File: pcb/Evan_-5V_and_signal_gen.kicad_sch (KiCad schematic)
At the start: 34 parts, among them IC1 TL7660IDGKR, IC2 TL081IDT, IC4 UA78M33CDCYG3, IC9 TL081IDT, J2 ESQ-126-39-L-D, J3 ESQ-126-39-L-D, U5 TPS2069CDBVR_MOSFET

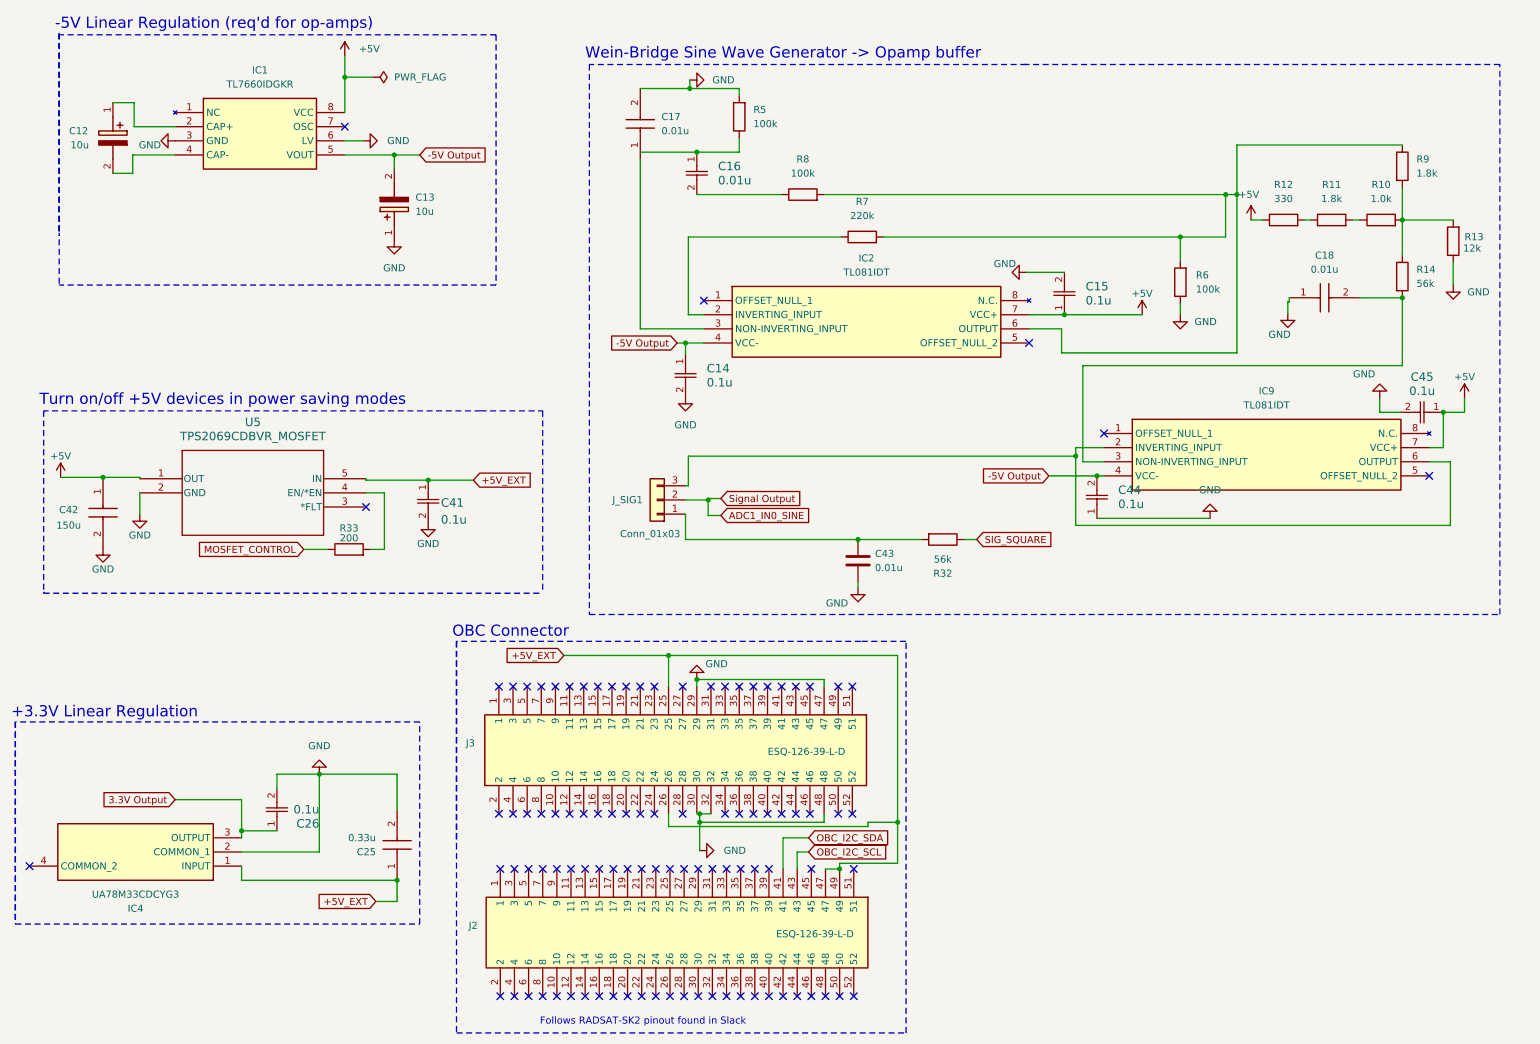
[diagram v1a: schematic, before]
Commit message: Added LM35 Temp Sensor
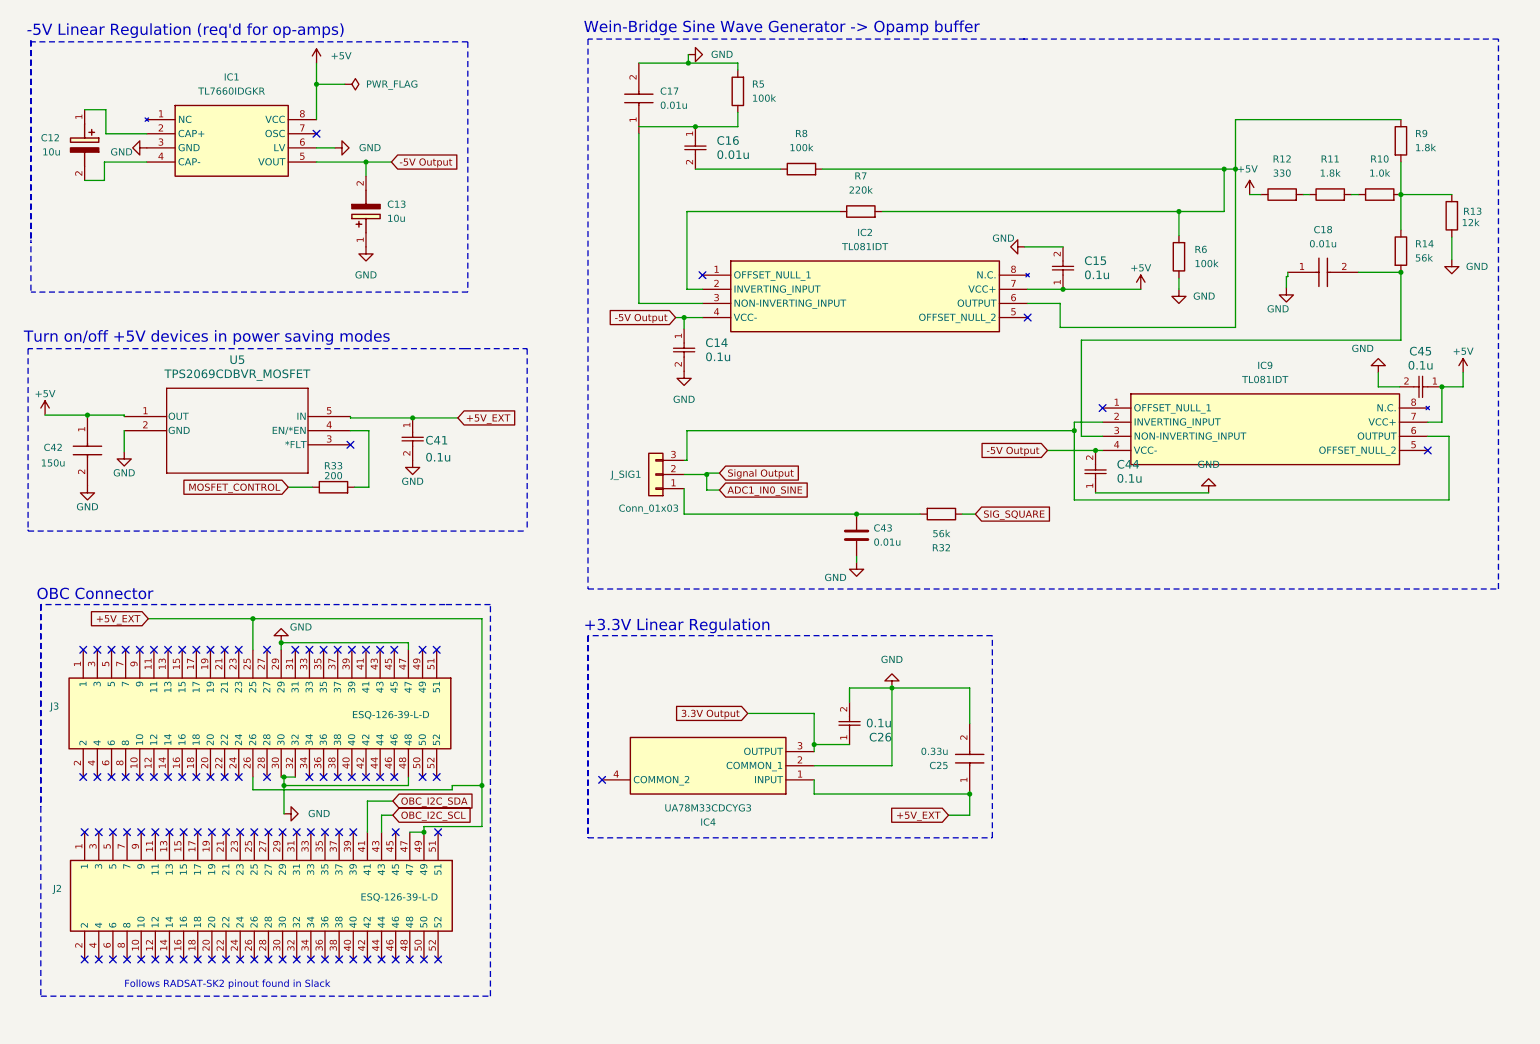
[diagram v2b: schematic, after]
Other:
- moved on the sheet: C12, C13, C14, C15, C16, C17, C18, C25, C26, C41, C42, C43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

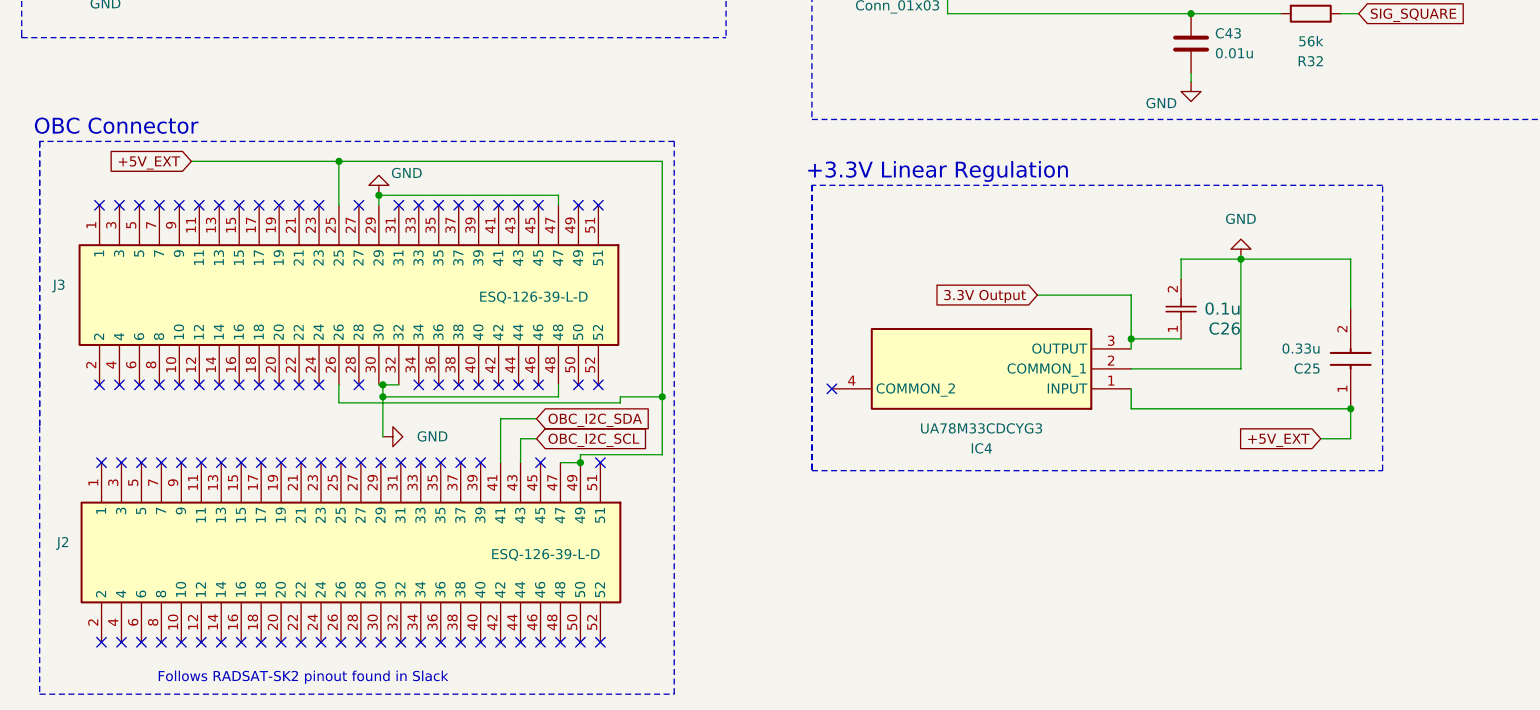
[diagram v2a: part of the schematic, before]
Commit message: Added GND and PWR planes
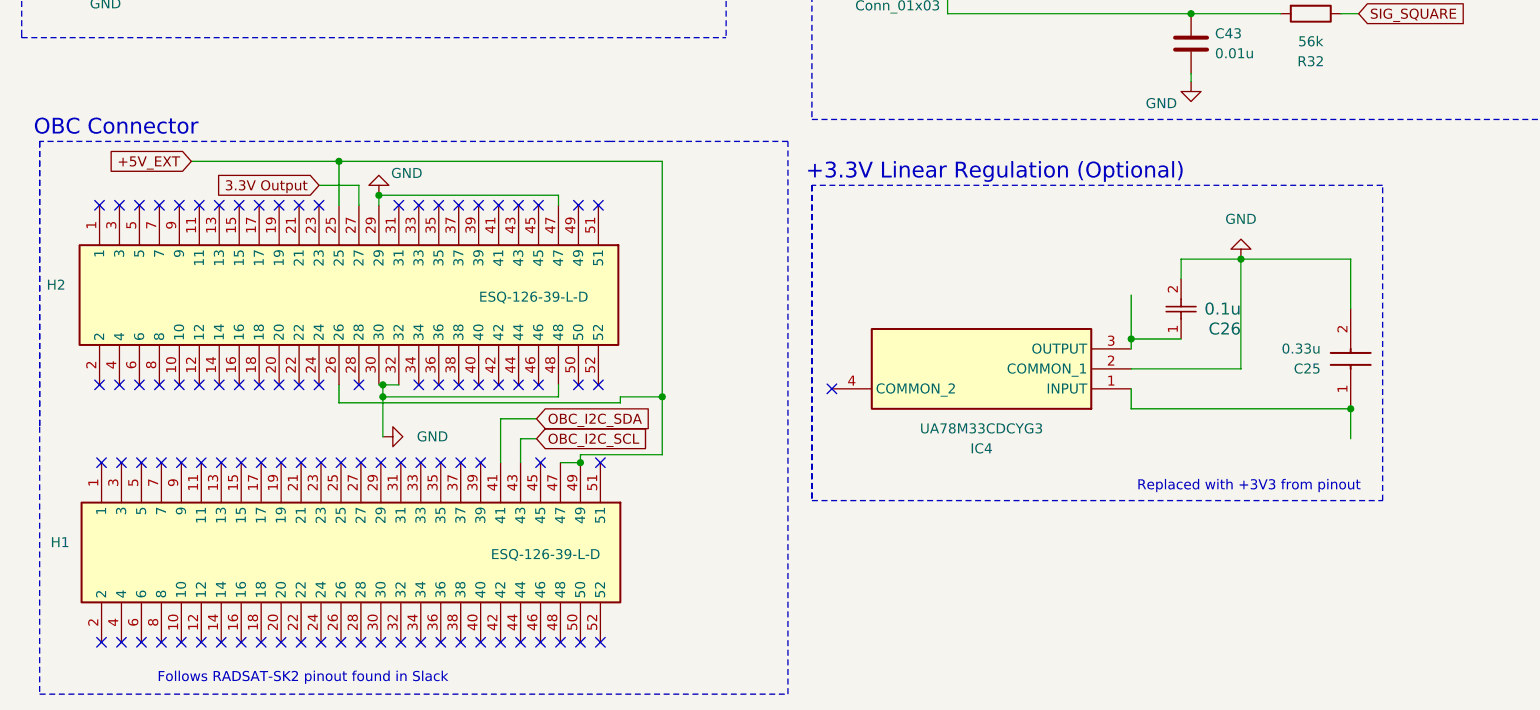
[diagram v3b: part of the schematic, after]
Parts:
- renumbered J2 to H1, J3 to H2
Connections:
- net +5V_EXT: no longer C25.1, IC4.1 (INPUT)
- net 3.3V Output: now also H2.27; no longer C26.1, IC4.3 (OUTPUT)
- new net: C26.1, IC4.3 (OUTPUT)
- new net: C25.1, IC4.1 (INPUT)
- no-connect marks 100 -> 99
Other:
- note added: "+3.3V Linear Regulation (Optional)"
- note added: "Replaced with +3V3 from pinout"
- note removed: "+3.3V Linear Regulation"
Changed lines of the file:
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@@
 	)
 	(no_connect
-		(at 59.69 127)
-	)
-	(no_connect
 		(at 82.55 127)
 	)
@@
 	(polyline
 		(pts
-			(xy 99.822 189.23) (xy 99.822 118.872)
+			(xy 114.3 189.23) (xy 114.3 118.872)
 		)
 		(stroke
@@
 	(polyline
 		(pts
-			(xy 189.992 160.782) (xy 189.992 124.46)
+			(xy 189.992 164.592) (xy 189.992 124.46)
 		)
 		(stroke
@@
 	(polyline
 		(pts
-			(xy 99.822 118.872) (xy 91.694 118.872)
+			(xy 114.3 118.872) (xy 91.694 118.872)
 		)
 		(stroke
@@
 	(wire
 		(pts
+			(xy 54.61 124.46) (xy 59.69 124.46)
+		)
+		(stroke
+			(width 0)
+			(type default)
+		)
+	)
+	(wire
+		(pts
 			(xy 263.398 45.212) (xy 263.398 51.562)
 		)
@@
 	(polyline
 		(pts
-			(xy 117.348 124.46) (xy 117.348 160.782)
+			(xy 117.348 124.46) (xy 117.348 164.592)
 		)
 		(stroke
@@
 	(polyline
 		(pts
-			(xy 19.05 189.23) (xy 99.822 189.23)
+			(xy 19.05 189.23) (xy 114.3 189.23)
 		)
 		(stroke
@@
 	(wire
 		(pts
-			(xy 157.988 138.43) (xy 146.05 138.43)
-		)
-		(stroke
-			(width 0)
-			(type default)
-		)
-	)
-	(wire
-		(pts
 			(xy 135.128 92.964) (xy 134.62 92.964)
 		)
@@
 	(polyline
 		(pts
-			(xy 117.348 160.782) (xy 189.992 160.782)
+			(xy 117.348 164.592) (xy 189.992 164.592)
 		)
 		(stroke
@@
 	(wire
 		(pts
-			(xy 182.118 156.718) (xy 185.928 156.718)
-		)
-		(stroke
-			(width 0)
-			(type default)
-		)
-	)
-	(wire
-		(pts
 			(xy 62.23 149.86) (xy 62.738 149.86)
 		)
@@
 	(polyline
 		(pts
-			(xy 117.348 124.46) (xy 117.348 160.782)
+			(xy 117.348 124.46) (xy 117.348 164.592)
 		)
 		(stroke
@@
 		)
 	)
+	(wire
+		(pts
+			(xy 59.69 124.46) (xy 59.69 127)
+		)
+		(stroke
+			(width 0)
+			(type default)
+		)
+	)
 	(polyline
 		(pts
@@
 		)
 	)
-	(text "+3.3V Linear Regulation"
+	(text "+3.3V Linear Regulation (Optional)"
 		(exclude_from_sim no)
 		(at 116.586 123.952 0)
@@
 		)
 	)
-	(global_label "+5V_EXT"
-		(shape input)
-		(at 182.118 156.718 180)
-		(fields_autoplaced yes)
+	(text "Replaced with +3V3 from pinout"
+		(exclude_from_sim no)
+		(at 172.974 162.814 0)
 		(effects
 			(font
 				(size 1.27 1.27)
 			)
-			(justify right)
-		)
-		(property "Intersheetrefs" "${INTERSHEET_REFS}"
-			(at 170.9686 156.718 0)
-			(effects
-				(font
-					(size 1.27 1.27)
-				)
-				(justify right)
-				(hide yes)
-			)
 		)
 	)
@@
 		)
 	)
+	(global_label "3.3V Output"
+		(shape input)
+		(at 54.61 124.46 180)
+		(fields_autoplaced yes)
+		(effects
+			(font
+				(size 1.27 1.27)
+			)
+			(justify right)
+		)
+		(property "Intersheetrefs" "${INTERSHEET_REFS}"
+			(at 40.3159 124.46 0)
+			(effects
+				(font
+					(size 1.27 1.27)
+				)
+				(justify right)
+				(hide yes)
+			)
+		)
+	)
 	(global_label "Signal Output"
 		(shape input)
@@
 		)
 	)
-	(global_label "3.3V Output"
-		(shape input)
-		(at 146.05 138.43 180)
-		(fields_autoplaced yes)
-		(effects
-			(font
-				(size 1.27 1.27)
-			)
-			(justify right)
-		)
-		(property "Intersheetrefs" "${INTERSHEET_REFS}"
-			(at 131.7559 138.43 0)
-			(effects
-				(font
-					(size 1.27 1.27)
-				)
-				(justify right)
-				(hide yes)
-			)
-		)
-	)
 	(global_label "-5V Output"
 		(shape input)
@@
 		(on_board yes)
 		(dnp no)
-		(property "Reference" "J2"
+		(property "Reference" "H1"
 			(at 22.86 169.926 90)
 			(effects
@@
 			(project "mcu_integration"
 				(path "/c0210bc3-f67f-47d8-a34e-f002a728adb2/39708197-8fe0-4b5c-ba49-65ed06982da9"
-					(reference "J2")
+					(reference "H1")
 					(unit 1)
 				)
@@
 		(on_board yes)
 		(dnp no)
-		(property "Reference" "J3"
+		(property "Reference" "H2"
 			(at 22.352 137.16 90)
 			(effects
@@
 			(project "mcu_integration"
 				(path "/c0210bc3-f67f-47d8-a34e-f002a728adb2/39708197-8fe0-4b5c-ba49-65ed06982da9"
-					(reference "J3")
+					(reference "H2")
 					(unit 1)
 				)

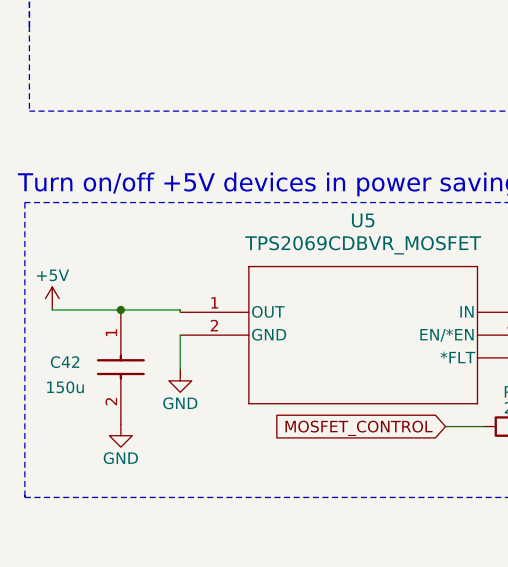
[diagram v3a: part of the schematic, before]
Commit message: Added +5v connections
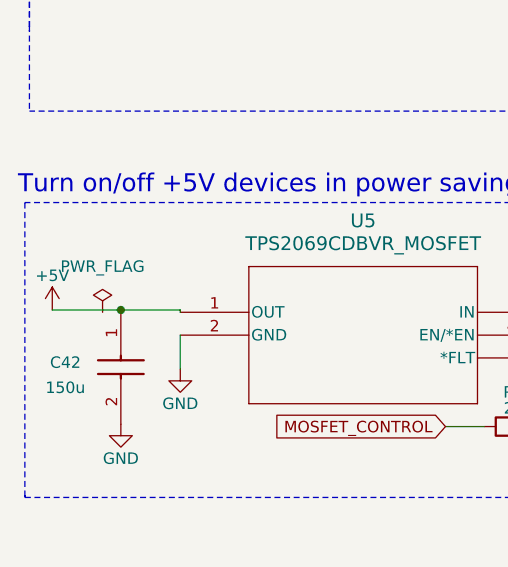
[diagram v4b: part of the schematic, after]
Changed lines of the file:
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@@
+	)
+	(symbol
+		(lib_name "PWR_FLAG_1")
+		(lib_id "power:PWR_FLAG")
+		(at 25.4 85.09 0)
+		(unit 1)
+		(exclude_from_sim no)
+		(in_bom yes)
+		(on_board yes)
+		(dnp no)
+		(fields_autoplaced yes)
+		(property "Reference" "#FLG04"
+			(at 25.4 83.185 0)
+			(effects
+				(font
+					(size 1.27 1.27)
+				)
+				(hide yes)
+			)
+		)
+		(property "Value" "PWR_FLAG"
+			(at 25.4 80.01 0)
+			(effects
+				(font
+					(size 1.27 1.27)
+				)
+			)
+		)
+		(property "Footprint" ""
+			(at 25.4 85.09 0)
+			(effects
+				(font
+					(size 1.27 1.27)
+				)
+				(hide yes)
+			)
+		)
+		(property "Datasheet" "~"
+			(at 25.4 85.09 0)
+			(effects
+				(font
+					(size 1.27 1.27)
+				)
+				(hide yes)
+			)
+		)
+		(property "Description" "Special symbol for telling ERC where power comes from"
+			(at 25.4 85.09 0)
+			(effects
+				(font
+					(size 1.27 1.27)
+				)
+				(hide yes)
+			)
+		)
+		(pin "1"
+		)
+		(instances
+			(project ""
+				(path "/c0210bc3-f67f-47d8-a34e-f002a728adb2/39708197-8fe0-4b5c-ba49-65ed06982da9"
+					(reference "#FLG04")
+					(unit 1)
+				)
+			)
+		)
 	)
 	(symbol
